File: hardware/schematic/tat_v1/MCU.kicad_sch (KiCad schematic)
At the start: 23 parts, among them J3 JST-SH 1x7P, SW2 SW_SPDT, SW3 SW_Push, U4 STM32U073CCUx, X1 32.768KHz

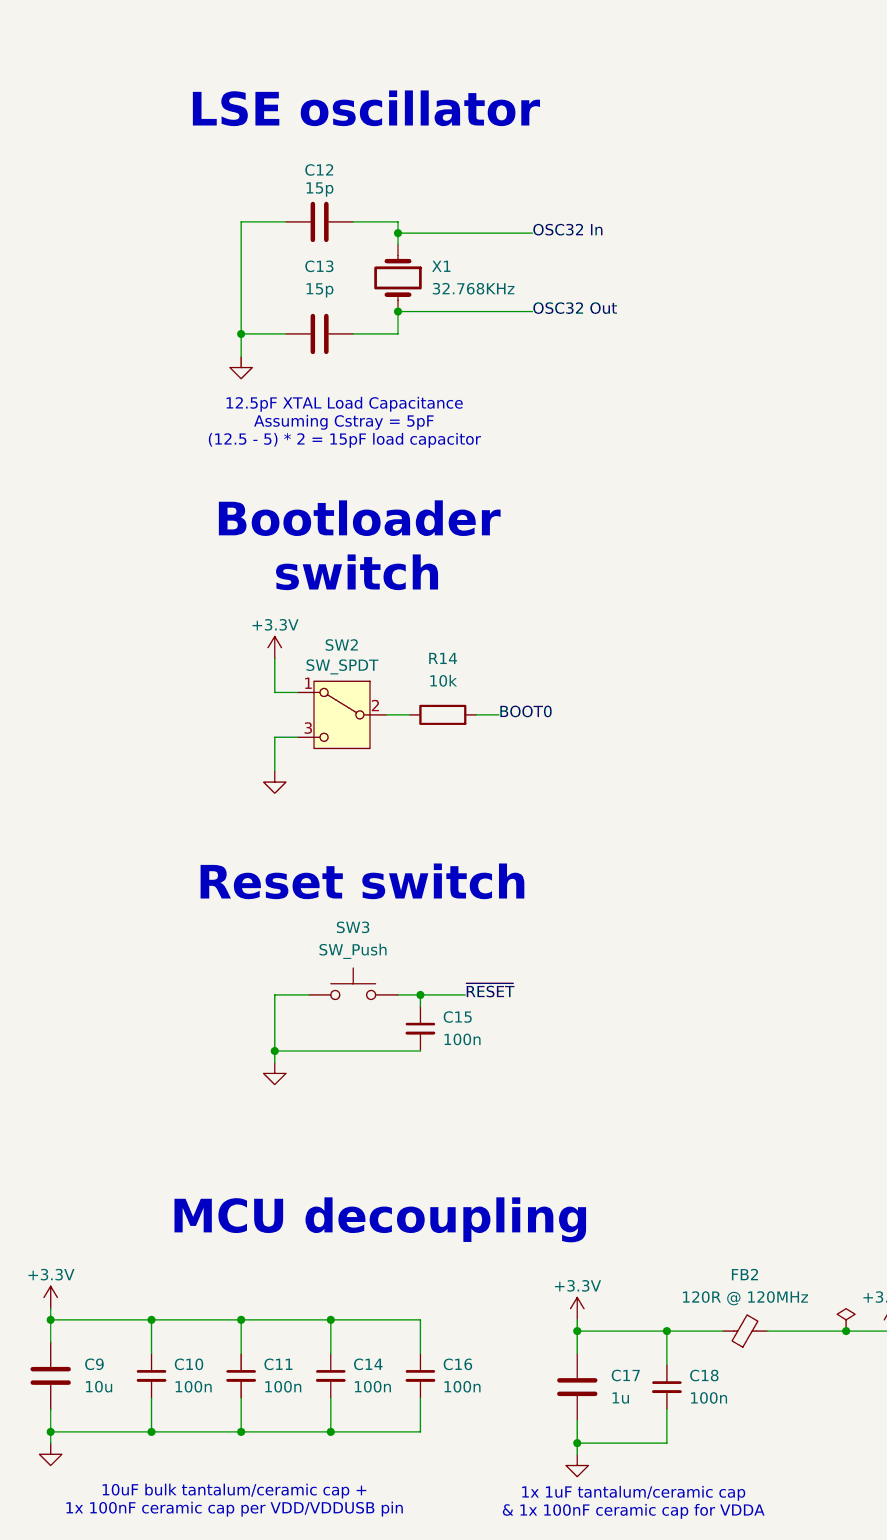
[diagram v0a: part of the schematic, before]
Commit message: Continuing with setting basic footprints for parts
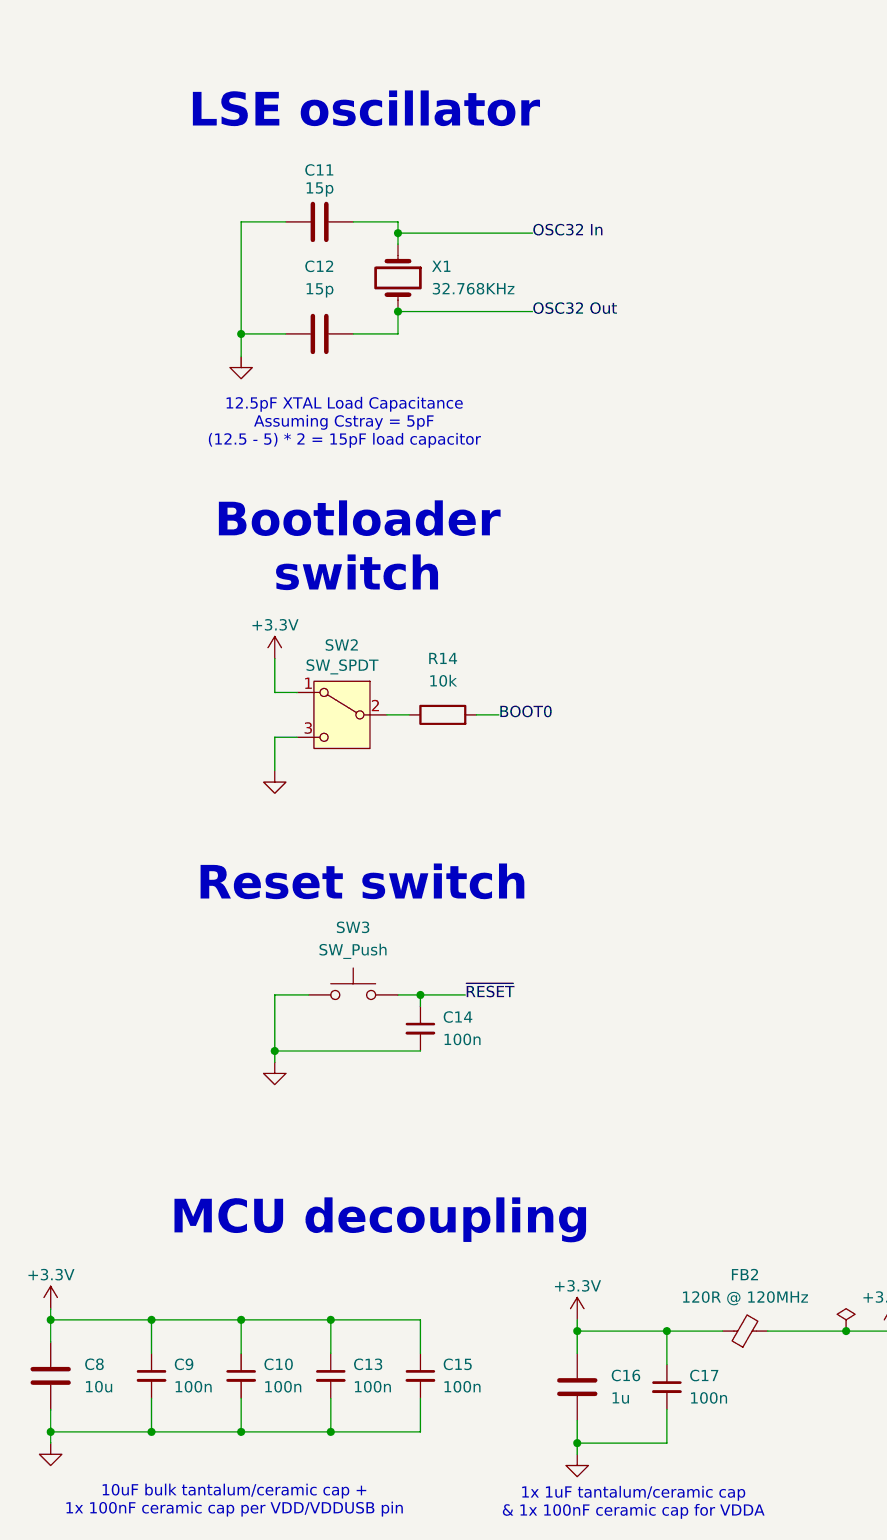
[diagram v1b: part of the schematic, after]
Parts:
- renumbered C11 to C10, C12 to C11, C13 to C12, C14 to C13, C15 to C14, C16 to C15, C17 to C16, C18 to C17, C9 to C8, C10 to C9
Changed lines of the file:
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@@
 		(dnp no)
 		(fields_autoplaced yes)
-		(property "Reference" "#PWR037"
+		(property "Reference" "#PWR036"
 			(at 252.73 71.12 0)
 			(effects
@@
 			(project "tat_v1"
 				(path "/b6d2ddf1-6792-45dd-afc9-29fd74d587ec/61278459-0872-433c-8091-dd4d841ee895"
-					(reference "#PWR037")
+					(reference "#PWR036")
 					(unit 1)
 				)
@@
 		(dnp no)
 		(fields_autoplaced yes)
-		(property "Reference" "#PWR034"
+		(property "Reference" "#PWR033"
 			(at 240.03 71.12 0)
 			(effects
@@
 			(project "tat_v1"
 				(path "/b6d2ddf1-6792-45dd-afc9-29fd74d587ec/61278459-0872-433c-8091-dd4d841ee895"
-					(reference "#PWR034")
+					(reference "#PWR033")
 					(unit 1)
 				)
@@
 		(dnp no)
 		(fields_autoplaced yes)
-		(property "Reference" "C18"
+		(property "Reference" "C17"
 			(at 97.79 171.4562 0)
 			(effects
@@
 			(project "tat_v1"
 				(path "/b6d2ddf1-6792-45dd-afc9-29fd74d587ec/61278459-0872-433c-8091-dd4d841ee895"
-					(reference "C18")
+					(reference "C17")
 					(unit 1)
 				)
@@
 		(dnp no)
 		(fields_autoplaced yes)
-		(property "Reference" "C15"
+		(property "Reference" "C14"
 			(at 69.85 130.8162 0)
 			(effects
@@
 			(project "tat_v1"
 				(path "/b6d2ddf1-6792-45dd-afc9-29fd74d587ec/61278459-0872-433c-8091-dd4d841ee895"
-					(reference "C15")
+					(reference "C14")
 					(unit 1)
 				)
@@
 		(dnp no)
 		(fields_autoplaced yes)
-		(property "Reference" "C9"
+		(property "Reference" "C8"
 			(at 29.21 170.1799 0)
 			(effects
@@
 			(project "tat_v1"
 				(path "/b6d2ddf1-6792-45dd-afc9-29fd74d587ec/61278459-0872-433c-8091-dd4d841ee895"
-					(reference "C9")
+					(reference "C8")
 					(unit 1)
 				)
@@
 		(on_board yes)
 		(dnp no)
-		(property "Reference" "#PWR020"
+		(property "Reference" "#PWR019"
 			(at 25.4 167.64 0)
 			(effects
@@
 			(project "tat_v1"
 				(path "/b6d2ddf1-6792-45dd-afc9-29fd74d587ec/61278459-0872-433c-8091-dd4d841ee895"
-					(reference "#PWR020")
+					(reference "#PWR019")
 					(unit 1)
 				)
@@
 		(on_board yes)
 		(dnp no)
-		(property "Reference" "C13"
+		(property "Reference" "C12"
 			(at 55.88 45.72 90)
 			(effects
@@
 			(project "tat_v1"
 				(path "/b6d2ddf1-6792-45dd-afc9-29fd74d587ec/61278459-0872-433c-8091-dd4d841ee895"
-					(reference "C13")
+					(reference "C12")
 					(unit 1)
 				)
@@
 		(dnp no)
 		(fields_autoplaced yes)
-		(property "Reference" "C16"
+		(property "Reference" "C15"
 			(at 69.85 170.1862 0)
 			(effects
@@
 			(project "tat_v1"
 				(path "/b6d2ddf1-6792-45dd-afc9-29fd74d587ec/61278459-0872-433c-8091-dd4d841ee895"
-					(reference "C16")
+					(reference "C15")
 					(unit 1)
 				)
@@
 		(on_board yes)
 		(dnp no)
-		(property "Reference" "#PWR032"
+		(property "Reference" "#PWR031"
 			(at 161.29 58.42 0)
 			(effects
@@
 			(project "tat_v1"
 				(path "/b6d2ddf1-6792-45dd-afc9-29fd74d587ec/61278459-0872-433c-8091-dd4d841ee895"
-					(reference "#PWR032")
+					(reference "#PWR031")
 					(unit 1)
 				)
@@
 		(dnp no)
 		(fields_autoplaced yes)
-		(property "Reference" "#PWR030"
+		(property "Reference" "#PWR029"
 			(at 153.67 144.78 0)
 			(effects
@@
 			(project "tat_v1"
 				(path "/b6d2ddf1-6792-45dd-afc9-29fd74d587ec/61278459-0872-433c-8091-dd4d841ee895"
-					(reference "#PWR030")
+					(reference "#PWR029")
 					(unit 1)
 				)
@@
 		(on_board yes)
 		(dnp no)
-		(property "Reference" "#PWR029"
+		(property "Reference" "#PWR028"
 			(at 148.59 58.42 0)
 			(effects
@@
 			(project "tat_v1"
 				(path "/b6d2ddf1-6792-45dd-afc9-29fd74d587ec/61278459-0872-433c-8091-dd4d841ee895"
-					(reference "#PWR029")
+					(reference "#PWR028")
 					(unit 1)
 				)
@@
 		(dnp no)
 		(fields_autoplaced yes)
-		(property "Reference" "#PWR033"
+		(property "Reference" "#PWR032"
 			(at 227.33 71.12 0)
 			(effects
@@
 			(project "tat_v1"
 				(path "/b6d2ddf1-6792-45dd-afc9-29fd74d587ec/61278459-0872-433c-8091-dd4d841ee895"
-					(reference "#PWR033")
+					(reference "#PWR032")
 					(unit 1)
 				)
@@
 		(dnp no)
 		(fields_autoplaced yes)
-		(property "Reference" "#PWR025"
+		(property "Reference" "#PWR024"
 			(at 50.8 142.24 0)
 			(effects
@@
 			(project "tat_v1"
 				(path "/b6d2ddf1-6792-45dd-afc9-29fd74d587ec/61278459-0872-433c-8091-dd4d841ee895"
-					(reference "#PWR025")
+					(reference "#PWR024")
 					(unit 1)
 				)
@@
 		(on_board yes)
 		(dnp no)
-		(property "Reference" "#PWR031"
+		(property "Reference" "#PWR030"
 			(at 156.21 54.61 0)
 			(effects
@@
 			(project "tat_v1"
 				(path "/b6d2ddf1-6792-45dd-afc9-29fd74d587ec/61278459-0872-433c-8091-dd4d841ee895"
-					(reference "#PWR031")
+					(reference "#PWR030")
 					(unit 1)
 				)
@@
 		(dnp no)
 		(fields_autoplaced yes)
-		(property "Reference" "#PWR021"
+		(property "Reference" "#PWR020"
 			(at 25.4 185.42 0)
 			(effects
@@
 			(project "tat_v1"
 				(path "/b6d2ddf1-6792-45dd-afc9-29fd74d587ec/61278459-0872-433c-8091-dd4d841ee895"
-					(reference "#PWR021")
+					(reference "#PWR020")
 					(unit 1)
 				)
@@
 		(on_board yes)
 		(dnp no)
-		(property "Reference" "#PWR028"
+		(property "Reference" "#PWR027"
 			(at 120.65 170.18 0)
 			(effects
@@
 			(project "tat_v1"
 				(path "/b6d2ddf1-6792-45dd-afc9-29fd74d587ec/61278459-0872-433c-8091-dd4d841ee895"
-					(reference "#PWR028")
+					(reference "#PWR027")
 					(unit 1)
 				)
@@
 		(dnp no)
 		(fields_autoplaced yes)
-		(property "Reference" "C14"
+		(property "Reference" "C13"
 			(at 59.69 170.1862 0)
 			(effects
@@
 			(project "tat_v1"
 				(path "/b6d2ddf1-6792-45dd-afc9-29fd74d587ec/61278459-0872-433c-8091-dd4d841ee895"
-					(reference "C14")
+					(reference "C13")
 					(unit 1)
 				)
@@
 		(on_board yes)
 		(dnp no)
-		(property "Reference" "C12"
+		(property "Reference" "C11"
 			(at 55.88 34.798 90)
 			(effects
@@
 			(project "tat_v1"
 				(path "/b6d2ddf1-6792-45dd-afc9-29fd74d587ec/61278459-0872-433c-8091-dd4d841ee895"
-					(reference "C12")
+					(reference "C11")
 					(unit 1)
 				)
@@
 		(dnp no)
 		(fields_autoplaced yes)
-		(property "Reference" "#PWR024"
+		(property "Reference" "#PWR023"
 			(at 50.8 109.22 0)
 			(effects
@@
 			(project "tat_v1"
 				(path "/b6d2ddf1-6792-45dd-afc9-29fd74d587ec/61278459-0872-433c-8091-dd4d841ee895"
-					(reference "#PWR024")
+					(reference "#PWR023")
 					(unit 1)
 				)
@@
 		(dnp no)
 		(fields_autoplaced yes)
-		(property "Reference" "#PWR027"
+		(property "Reference" "#PWR026"
 			(at 85.09 186.69 0)
 			(effects
@@
 			(project "tat_v1"
 				(path "/b6d2ddf1-6792-45dd-afc9-29fd74d587ec/61278459-0872-433c-8091-dd4d841ee895"
-					(reference "#PWR027")
+					(reference "#PWR026")
 					(unit 1)
 				)
@@
 		(dnp no)
 		(fields_autoplaced yes)
-		(property "Reference" "#PWR036"
+		(property "Reference" "#PWR035"
 			(at 250.19 106.68 0)
 			(effects
@@
 			(project "tat_v1"
 				(path "/b6d2ddf1-6792-45dd-afc9-29fd74d587ec/61278459-0872-433c-8091-dd4d841ee895"
-					(reference "#PWR036")
+					(reference "#PWR035")
 					(unit 1)
 				)
@@
 		(dnp no)
 		(fields_autoplaced yes)
-		(property "Reference" "C17"
+		(property "Reference" "C16"
 			(at 88.9 171.4499 0)
 			(effects
@@
 			(project "tat_v1"
 				(path "/b6d2ddf1-6792-45dd-afc9-29fd74d587ec/61278459-0872-433c-8091-dd4d841ee895"
-					(reference "C17")
+					(reference "C16")
 					(unit 1)
 				)
@@
 		(dnp no)
 		(fields_autoplaced yes)
-		(property "Reference" "C10"
+		(property "Reference" "C9"
 			(at 39.37 170.1862 0)
 			(effects
@@
 			(project "tat_v1"
 				(path "/b6d2ddf1-6792-45dd-afc9-29fd74d587ec/61278459-0872-433c-8091-dd4d841ee895"
-					(reference "C10")
+					(reference "C9")
 					(unit 1)
 				)
@@
 		(on_board yes)
 		(dnp no)
-		(property "Reference" "#PWR023"
+		(property "Reference" "#PWR022"
 			(at 50.8 93.98 0)
 			(effects
@@
 			(project "tat_v1"
 				(path "/b6d2ddf1-6792-45dd-afc9-29fd74d587ec/61278459-0872-433c-8091-dd4d841ee895"
-					(reference "#PWR023")
+					(reference "#PWR022")
 					(unit 1)
 				)
@@
 		(on_board yes)
 		(dnp no)
-		(property "Reference" "#PWR026"
+		(property "Reference" "#PWR025"
 			(at 85.09 168.91 0)
 			(effects
@@
 			(project "tat_v1"
 				(path "/b6d2ddf1-6792-45dd-afc9-29fd74d587ec/61278459-0872-433c-8091-dd4d841ee895"
-					(reference "#PWR026")
+					(reference "#PWR025")
 					(unit 1)
 				)
@@
 		(on_board yes)
 		(dnp no)
-		(property "Reference" "#PWR035"
+		(property "Reference" "#PWR034"
 			(at 250.19 97.79 0)
 			(effects
@@
 			(project "tat_v1"
 				(path "/b6d2ddf1-6792-45dd-afc9-29fd74d587ec/61278459-0872-433c-8091-dd4d841ee895"
-					(reference "#PWR035")
+					(reference "#PWR034")
 					(unit 1)
 				)
@@
 		(dnp no)
 		(fields_autoplaced yes)
-		(property "Reference" "#PWR022"
+		(property "Reference" "#PWR021"
 			(at 46.99 62.23 0)
 			(effects
@@
 			(project "tat_v1"
 				(path "/b6d2ddf1-6792-45dd-afc9-29fd74d587ec/61278459-0872-433c-8091-dd4d841ee895"
-					(reference "#PWR022")
+					(reference "#PWR021")
 					(unit 1)
 				)
@@
 		(dnp no)
 		(fields_autoplaced yes)
-		(property "Reference" "C11"
+		(property "Reference" "C10"
 			(at 49.53 170.1862 0)
 			(effects
@@
 			(project "tat_v1"
 				(path "/b6d2ddf1-6792-45dd-afc9-29fd74d587ec/61278459-0872-433c-8091-dd4d841ee895"
-					(reference "C11")
-					(unit 1)
-				)
+					(reference "C10")
+					(unit 1)
+				)

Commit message: Continuing work on setting parts footprints
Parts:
- C11, C12, C14: footprint (none) -> Capacitor_SMD:C_0402_1005Metric
- R14: footprint (none) -> Resistor_SMD:R_0402_1005Metric; Link (none) -> https://www.lcsc.com/product-detail/Chip-Resistor-Surface-M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
- R15, R16, R17: footprint (none) -> Resistor_SMD:R_0402_1005Metric
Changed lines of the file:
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@@
 			)
 		)
-		(property "Footprint" ""
+		(property "Footprint" "Capacitor_SMD:C_0402_1005Metric"
 			(at 67.31 132.08 0)
 			(effects
@@
 			)
 		)
-		(property "Footprint" ""
+		(property "Footprint" "Resistor_SMD:R_0402_1005Metric"
 			(at 225.552 57.15 90)
 			(effects
@@
 			)
 		)
-		(property "Description" "Unpolarized capacitor"
+		(property "Description" "Tantalum capacitor"
 			(at 25.4 171.45 0)
 			(effects
@@
 			)
 		)
-		(property "Footprint" ""
+		(property "Footprint" "Resistor_SMD:R_0402_1005Metric"
 			(at 69.85 98.298 90)
 			(effects
@@
 			)
 		)
-		(property "Datasheet" "~"
+		(property "Datasheet" "https://www.lcsc.com/datasheet/lcsc_datasheet_2411221126_UNI-ROYAL-Uniroyal-Elec-0402WGF1002TCE_C25744.pdf"
 			(at 69.85 96.52 0)
 			(effects
@@
 			)
 		)
+		(property "Link" "https://www.lcsc.com/product-detail/Chip-Resistor-Surface-Mount_UNI-ROYAL-Uniroyal-Elec-0402WGF1002TCE_C25744.html"
+			(at 69.85 96.52 90)
+			(effects
+				(font
+					(size 1.27 1.27)
+				)
+				(hide yes)
+			)
+		)
 		(pin "2"
 		)
@@
 			)
 		)
-		(property "Footprint" ""
+		(property "Footprint" "Capacitor_SMD:C_0402_1005Metric"
 			(at 59.69 52.3748 0)
 			(effects
@@
 			)
 		)
-		(property "Footprint" ""
+		(property "Footprint" "Capacitor_SMD:C_0402_1005Metric"
 			(at 59.69 39.6748 0)
 			(effects
@@
 			)
 		)
-		(property "Footprint" ""
+		(property "Footprint" "Resistor_SMD:R_0402_1005Metric"
 			(at 250.952 57.15 90)
 			(effects
@@
 			)
 		)
-		(property "Footprint" ""
+		(property "Footprint" "Resistor_SMD:R_0402_1005Metric"
 			(at 238.252 57.15 90)
 			(effects
